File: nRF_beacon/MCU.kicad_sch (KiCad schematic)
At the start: 22 parts, among them U1 nRF54L15-QFAA, X1 32MHz, X2 32.768 kHz

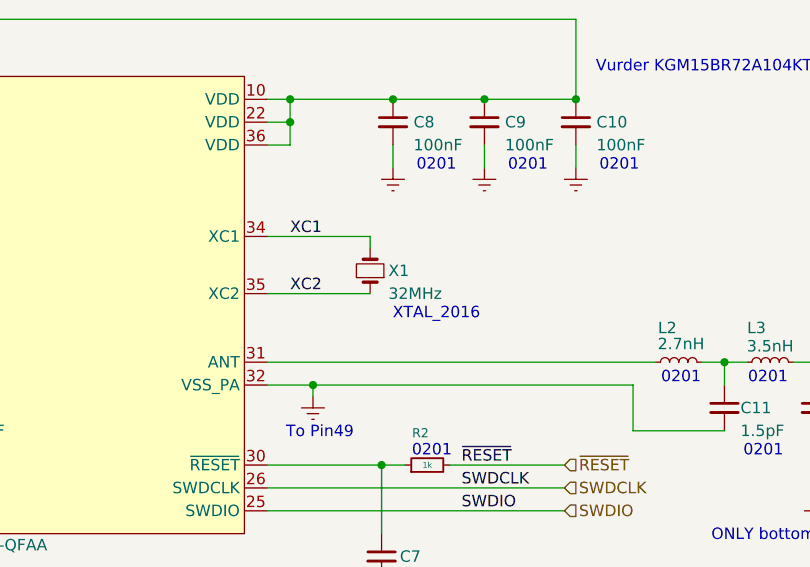
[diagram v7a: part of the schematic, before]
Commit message: Added most of the components to nRF54 typical application layout
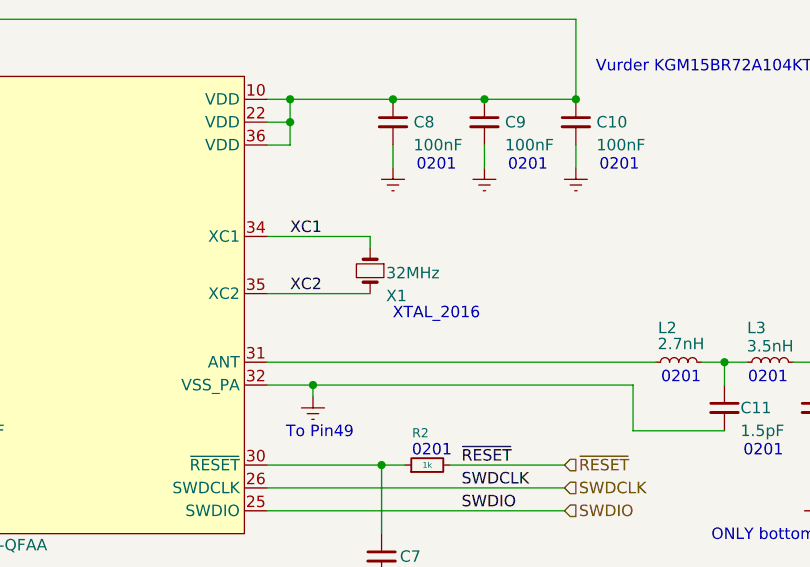
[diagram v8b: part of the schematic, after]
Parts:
- X1: footprint Crystal:Crystal_SMD_2016-4Pin_2.0x1.6mm -> Ekse:CX2016DB32000D0WZRC1
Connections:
- net XC1: now also X1.1; no longer X1.2
- net XC2: now also X1.3; no longer X1.1
- net Earth renamed GND
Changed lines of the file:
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@@
 			)
 		)
-		(property "Value" "Earth"
+		(property "Value" "GND"
 			(at 104.14 99.06 0)
 			(effects
@@
 			)
 		)
-		(property "Description" "Power symbol creates a global label with name \"Earth\""
+		(property "Description" "Power symbol creates a global label with name \"GND\""
 			(at 104.14 93.98 0)
 			(effects
@@
 			)
 		)
-		(property "Value" "Earth"
+		(property "Value" "GND"
 			(at 105.41 50.8 0)
 			(effects
@@
 			)
 		)
-		(property "Description" "Power symbol creates a global label with name \"Earth\""
+		(property "Description" "Power symbol creates a global label with name \"GND\""
 			(at 105.41 45.72 0)
 			(effects
@@
 			)
 		)
-		(property "Value" "Earth"
+		(property "Value" "GND"
 			(at 29.21 92.71 0)
 			(effects
@@
 			)
 		)
-		(property "Description" "Power symbol creates a global label with name \"Earth\""
+		(property "Description" "Power symbol creates a global label with name \"GND\""
 			(at 29.21 87.63 0)
 			(effects
@@
 			)
 		)
-		(property "Value" "Earth"
+		(property "Value" "GND"
 			(at 115.57 50.8 0)
 			(effects
@@
 			)
 		)
-		(property "Description" "Power symbol creates a global label with name \"Earth\""
+		(property "Description" "Power symbol creates a global label with name \"GND\""
 			(at 115.57 45.72 0)
 			(effects
@@
 			)
 		)
-		(property "Value" "Earth"
+		(property "Value" "GND"
 			(at 152.4 87.63 0)
 			(effects
@@
 			)
 		)
-		(property "Description" "Power symbol creates a global label with name \"Earth\""
+		(property "Description" "Power symbol creates a global label with name \"GND\""
 			(at 152.4 82.55 0)
 			(effects
@@
 			)
 		)
-		(property "Value" "Earth"
+		(property "Value" "GND"
 			(at 96.52 76.2 0)
 			(effects
@@
 			)
 		)
-		(property "Description" "Power symbol creates a global label with name \"Earth\""
+		(property "Description" "Power symbol creates a global label with name \"GND\""
 			(at 96.52 71.12 0)
 			(effects
@@
 			)
 		)
-		(property "Value" "Earth"
+		(property "Value" "GND"
 			(at 38.1 92.71 0)
 			(effects
@@
 			)
 		)
-		(property "Description" "Power symbol creates a global label with name \"Earth\""
+		(property "Description" "Power symbol creates a global label with name \"GND\""
 			(at 38.1 87.63 0)
 			(effects
@@
 			)
 		)
-		(property "Value" "Earth"
+		(property "Value" "GND"
 			(at 31.75 50.8 0)
 			(effects
@@
 			)
 		)
-		(property "Description" "Power symbol creates a global label with name \"Earth\""
+		(property "Description" "Power symbol creates a global label with name \"GND\""
 			(at 31.75 45.72 0)
 			(effects
@@
 			)
 		)
-		(property "Value" "Earth"
+		(property "Value" "GND"
 			(at 21.59 50.8 0)
 			(effects
@@
 			)
 		)
-		(property "Description" "Power symbol creates a global label with name \"Earth\""
+		(property "Description" "Power symbol creates a global label with name \"GND\""
 			(at 21.59 45.72 0)
 			(effects
@@
 			)
 		)
-		(property "Value" "Earth"
+		(property "Value" "GND"
 			(at 19.05 92.71 0)
 			(effects
@@
 			)
 		)
-		(property "Description" "Power symbol creates a global label with name \"Earth\""
+		(property "Description" "Power symbol creates a global label with name \"GND\""
 			(at 19.05 87.63 0)
 			(effects
@@
 			)
 		)
-		(property "Value" "Earth"
+		(property "Value" "GND"
 			(at 46.99 73.66 0)
 			(effects
@@
 			)
 		)
-		(property "Description" "Power symbol creates a global label with name \"Earth\""
+		(property "Description" "Power symbol creates a global label with name \"GND\""
 			(at 46.99 68.58 0)
 			(effects
@@
 			)
 		)
-		(property "Value" "Earth"
+		(property "Value" "GND"
 			(at 49.53 92.71 0)
 			(effects
@@
 			)
 		)
-		(property "Description" "Power symbol creates a global label with name \"Earth\""
+		(property "Description" "Power symbol creates a global label with name \"GND\""
 			(at 49.53 87.63 0)
 			(effects
@@
 			)
 		)
-		(property "Value" "Earth"
+		(property "Value" "GND"
 			(at 162.56 83.82 0)
 			(effects
@@
 			)
 		)
-		(property "Description" "Power symbol creates a global label with name \"Earth\""
+		(property "Description" "Power symbol creates a global label with name \"GND\""
 			(at 162.56 78.74 0)
 			(effects
@@
 			)
 		)
-		(property "Value" "Earth"
+		(property "Value" "GND"
 			(at 125.73 50.8 0)
 			(effects
@@
 			)
 		)
-		(property "Description" "Power symbol creates a global label with name \"Earth\""
+		(property "Description" "Power symbol creates a global label with name \"GND\""
 			(at 125.73 45.72 0)
 			(effects
@@
 	)
 	(symbol
+		(lib_name "Crystal_Small_1")
 		(lib_id "Device:Crystal_Small")
 		(at 102.87 57.15 90)
+		(mirror x)
 		(unit 1)
 		(exclude_from_sim no)
@@
 		(dnp no)
 		(property "Reference" "X1"
-			(at 104.902 57.15 90)
+			(at 104.648 59.944 90)
 			(effects
 				(font
@@
 		)
 		(property "Value" "32MHz"
-			(at 104.902 59.69 90)
+			(at 104.648 57.404 90)
 			(effects
 				(font
@@
 			)
 		)
-		(property "Footprint" "Crystal:Crystal_SMD_2016-4Pin_2.0x1.6mm"
+		(property "Footprint" "Ekse:CX2016DB32000D0WZRC1"
 			(at 102.87 57.15 0)
 			(effects
@@
 			)
 		)
-		(pin "2"
+		(pin "3"
 		)
 		(pin "1"
